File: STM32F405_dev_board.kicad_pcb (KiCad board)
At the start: 4 copper layers, 39.4 x 83.8 mm, 46 parts, among them IC2 FT232RNL-REEL, J1 Conn_ARM_JTAG_SWD_20, J2 Conn_01x20_Pin, J3 Conn_01x20_Pin, J6 USB4800-03-A, U1 STM32F405RGT6, Y1 8MHz, Y2 Crystal_GND23

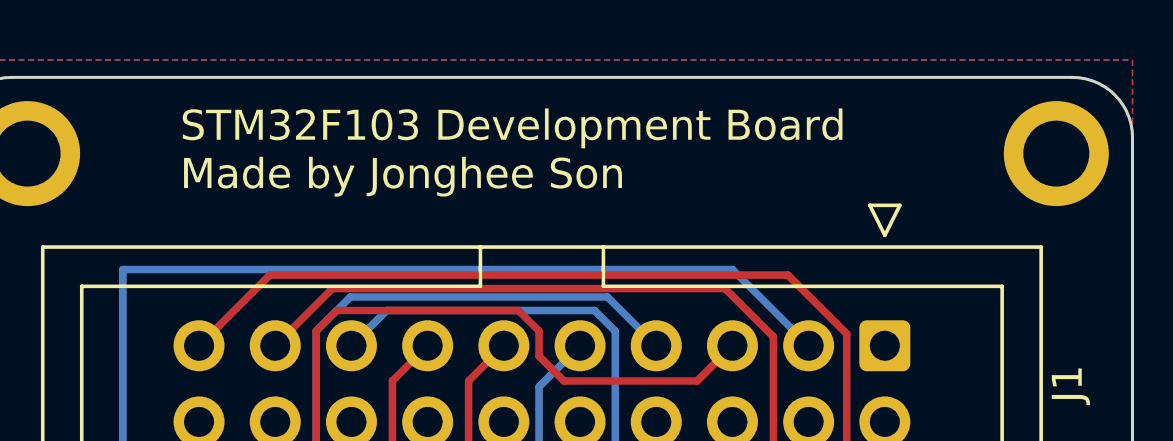
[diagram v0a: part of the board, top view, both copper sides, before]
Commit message: Changed board marking
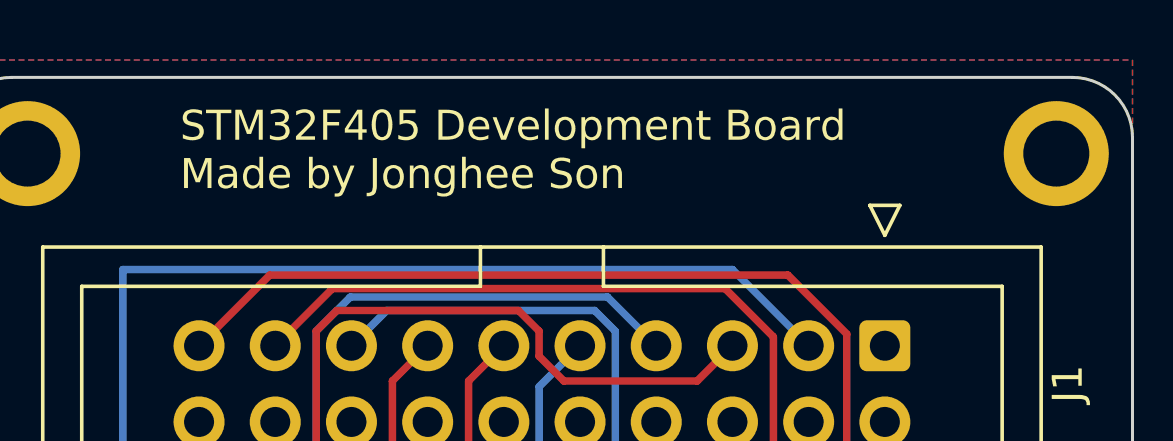
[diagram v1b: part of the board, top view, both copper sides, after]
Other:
- board text added: "STM32F405 Development Board Made by Jonghee Son"
- board text removed: "STM32F103 Development Board Made by Jonghee Son"
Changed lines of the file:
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@@
     (effects (font (size 1 1) (thickness 0.15)) (justify left bottom))
   )
-  (gr_text "STM32F103 Development Board\nMade by Jonghee Son" (at 133.35 61.54) (layer "F.SilkS")
+  (gr_text "STM32F405 Development Board\nMade by Jonghee Son" (at 133.35 61.54) (layer "F.SilkS")
     (effects (font (size 1 1) (thickness 0.15)) (justify left bottom))
   )
